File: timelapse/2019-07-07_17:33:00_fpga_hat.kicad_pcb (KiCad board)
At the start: 4 copper layers, 65 x 56.5 mm, 92 parts, among them J1 2x20, J2 AudioJack3, J3 Conn_02x06_Top_Bottom, J4 Conn_02x06_Top_Bottom, J5 Conn_02x06_Top_Bottom, J6 Conn_01x02, SW1 PTS815, SW2 PTS815, SW3 PTS815, SW4 PTS815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

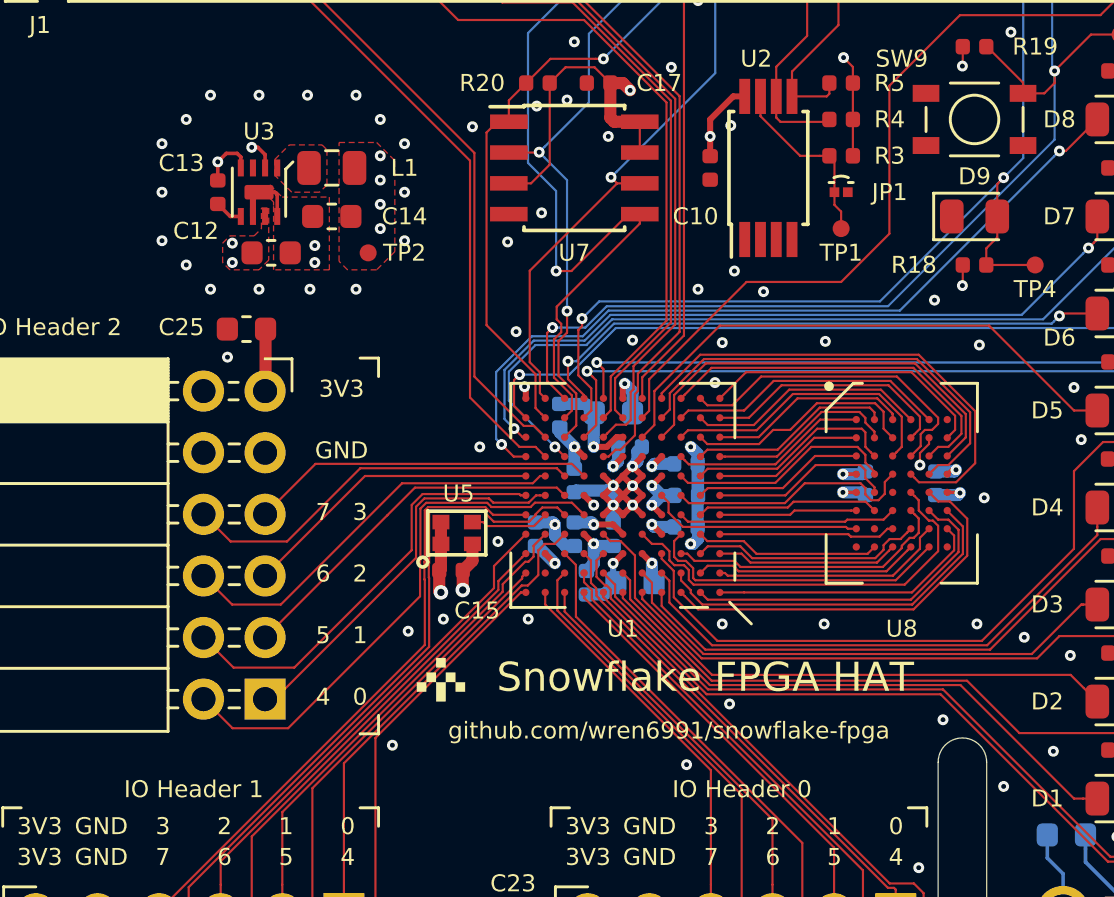
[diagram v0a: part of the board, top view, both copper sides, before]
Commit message: Rename board. Some silkscreen tweaks.
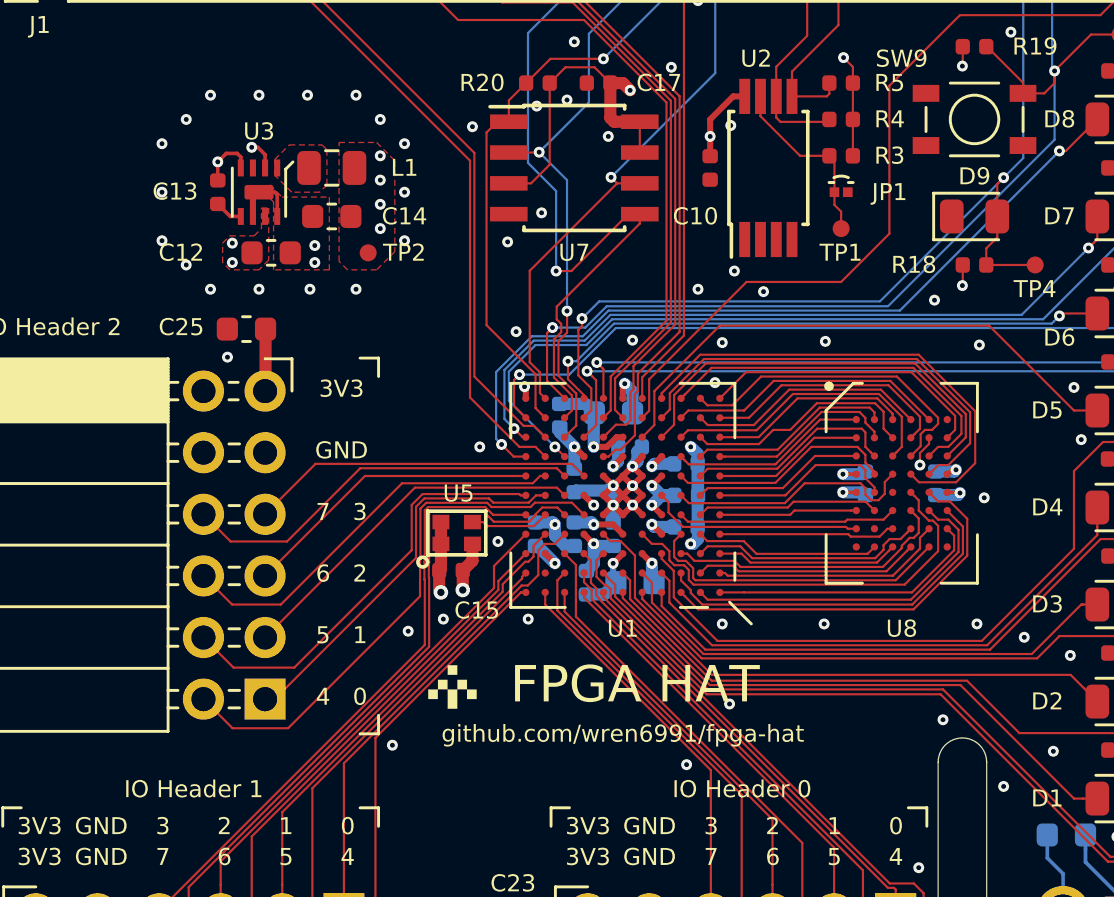
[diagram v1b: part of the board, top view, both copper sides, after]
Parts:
- moved REF** 0.56 mm to (125.5, 114.3)
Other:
- board text added: "FPGA HAT"
- board text added: "github.com/wren6991/fpga-hat"
- board text removed: "Rev A"
- board text removed: "Snowflake FPGA HAT"
- board text removed: "github.com/wren6991/snowflake-fpga"
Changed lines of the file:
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@@
   (general
     (thickness 1.6)
-    (drawings 75)
+    (drawings 74)
     (tracks 1244)
     (zones 0)
@@
     (34 B.Paste user hide)
     (35 F.Paste user hide)
-    (36 B.SilkS user)
+    (36 B.SilkS user hide)
     (37 F.SilkS user)
     (38 B.Mask user hide)
@@
   )
   (module fpga_hat:github_avatar (layer F.Cu)
-    (at 125 114)
+    (at 125.476 114.3)
     (fp_text reference REF** (at 0 0.5) (layer F.SilkS) hide
       (effects (font (size 0.03 0.03) (thickness 0.0075)))
@@
     (tags capacitor)
     (attr smd)
-    (fp_text reference C8 (at 0.5 -1.2 180) (layer B.SilkS)
+    (fp_text reference C8 (at -0.1 -1.3 180) (layer B.SilkS)
       (effects (font (size 0.7 0.7) (thickness 0.12)) (justify mirror))
     )
@@
     (tags capacitor)
     (attr smd)
-    (fp_text reference C2 (at 2.1875 -0.3) (layer B.SilkS)
+    (fp_text reference C2 (at 2.3875 -0.1) (layer B.SilkS)
       (effects (font (size 0.7 0.7) (thickness 0.12)) (justify mirror))
     )
@@
     (tags capacitor)
     (attr smd)
-    (fp_text reference C11 (at 1.8 -0.6) (layer B.SilkS)
+    (fp_text reference C11 (at 1.7 -0.5) (layer B.SilkS)
       (effects (font (size 0.7 0.7) (thickness 0.12)) (justify mirror))
     )
@@
     (tags capacitor)
     (attr smd)
-    (fp_text reference C12 (at -3.1 -0.9) (layer F.SilkS)
+    (fp_text reference C12 (at -3.7 0) (layer F.SilkS)
       (effects (font (size 0.7 0.7) (thickness 0.12)))
     )
@@
     (tags capacitor)
     (attr smd)
-    (fp_text reference C13 (at -1.2 1.5 180) (layer F.SilkS)
+    (fp_text reference C13 (at -0.02 1.754 180) (layer F.SilkS)
       (effects (font (size 0.7 0.7) (thickness 0.12)))
     )
@@
     )
   )
-  (gr_text "Rev A" (at 137.6 131.2) (layer B.SilkS)
-    (effects (font (size 1 1) (thickness 0.15)) (justify mirror))
-  )
   (gr_text GND (at 120.904 104.648) (layer F.SilkS)
     (effects (font (size 0.7 0.7) (thickness 0.12)))
@@
   )
   (gr_line (start 129.6 106.8) (end 130 107.2) (layer B.SilkS) (width 0.12))
-  (gr_text github.com/wren6991/snowflake-fpga (at 134.4 116.2) (layer F.SilkS)
+  (gr_text github.com/wren6991/fpga-hat (at 132.5 116.332) (layer F.SilkS)
     (effects (font (size 0.7 0.7) (thickness 0.12)))
   )
-  (gr_text "Snowflake FPGA HAT" (at 135.9 114) (layer F.SilkS)
-    (effects (font (size 1.2 1.2) (thickness 0.17)))
+  (gr_text "FPGA HAT" (at 133 114.3) (layer F.SilkS)
+    (effects (font (size 1.5 1.5) (thickness 0.2)))
   )
   (gr_line (start 100 121) (end 100 133.5) (layer Edge.Cuts) (width 0.05))
